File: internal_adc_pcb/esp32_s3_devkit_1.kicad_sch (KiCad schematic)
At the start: 2 parts, among them J1 Conn_01x22, J2 Conn_01x22

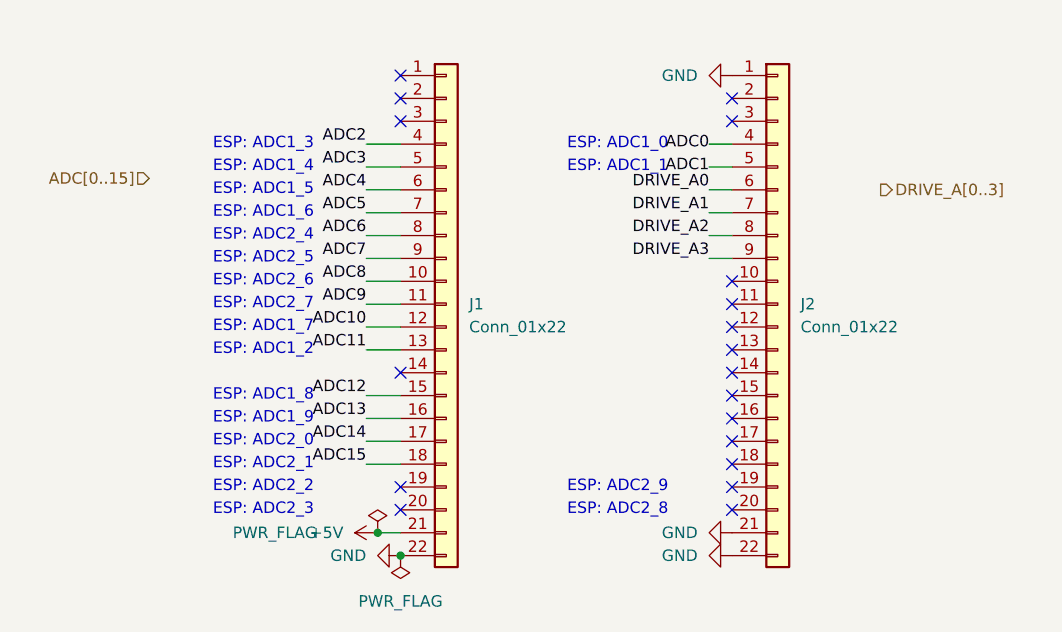
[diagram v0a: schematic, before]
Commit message: done all 4 TIA opamps for internal adc version
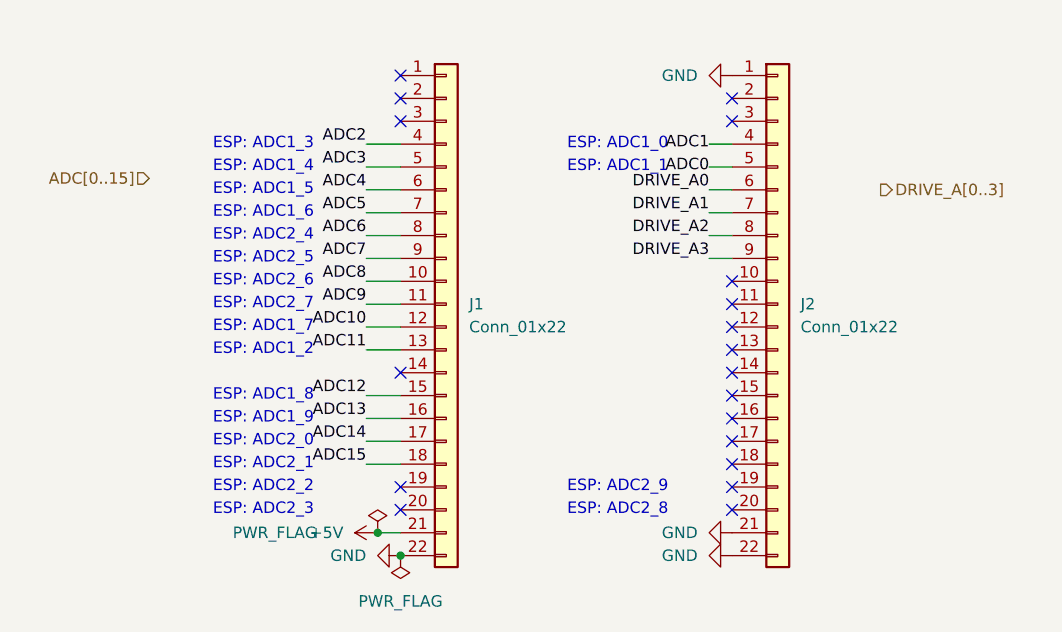
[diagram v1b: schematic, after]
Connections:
- net ADC0: now also J2.5 (Pin_5); no longer J2.4 (Pin_4)
- net ADC1: now also J2.4 (Pin_4); no longer J2.5 (Pin_5)
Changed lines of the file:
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@@
 		)
 	)
-	(label "ADC0"
+	(label "ADC1"
 		(at 92.71 64.77 180)
 		(effects
@@
 		)
 	)
-	(label "ADC1"
+	(label "ADC0"
 		(at 92.71 67.31 180)
 		(effects

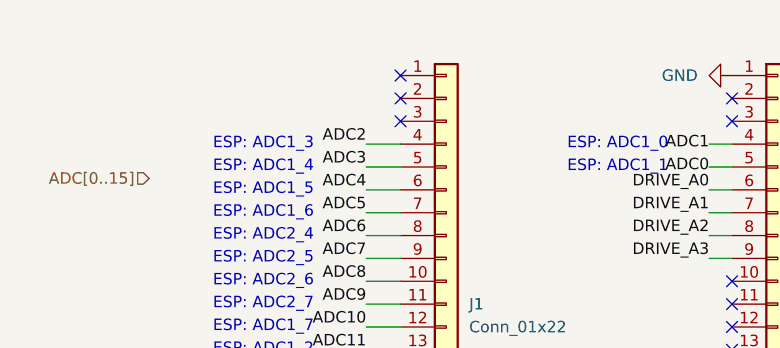
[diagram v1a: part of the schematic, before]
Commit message: fixing all ERC errors for internal ADC ver, fixing warnings now
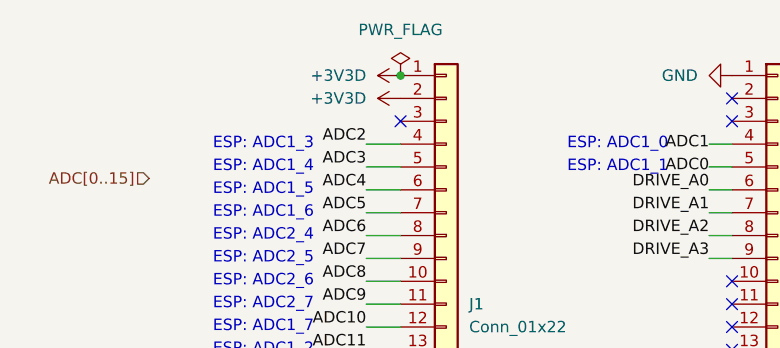
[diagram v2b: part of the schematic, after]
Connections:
- net +3V3D: now reaches J1.1 (Pin_1)
- net +3V3D: now also J1.2 (Pin_2)
- no-connect marks 19 -> 17
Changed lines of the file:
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@@
+	)
+	(junction
+		(at 58.42 57.15)
+		(diameter 0)
+		(color 0 0 0 0)
 	)
 	(junction
@@
 	(no_connect
 		(at 95.25 62.23)
-	)
-	(no_connect
-		(at 58.42 59.69)
-	)
-	(no_connect
-		(at 58.42 57.15)
 	)
 	(no_connect
@@
 	(symbol
 		(lib_id "power:PWR_FLAG")
+		(at 58.42 57.15 0)
+		(unit 1)
+		(body_style 1)
+		(exclude_from_sim no)
+		(in_bom yes)
+		(on_board yes)
+		(in_pos_files yes)
+		(dnp no)
+		(fields_autoplaced yes)
+		(property "Reference" "#FLG03"
+			(at 58.42 55.245 0)
+			(hide yes)
+			(show_name no)
+			(do_not_autoplace no)
+			(effects
+				(font
+					(size 1.27 1.27)
+				)
+			)
+		)
+		(property "Value" "PWR_FLAG"
+			(at 58.42 52.07 0)
+			(show_name no)
+			(do_not_autoplace no)
+			(effects
+				(font
+					(size 1.27 1.27)
+				)
+			)
+		)
+		(property "Footprint" ""
+			(at 58.42 57.15 0)
+			(hide yes)
+			(show_name no)
+			(do_not_autoplace no)
+			(effects
+				(font
+					(size 1.27 1.27)
+				)
+			)
+		)
+		(property "Datasheet" ""
+			(at 58.42 57.15 0)
+			(hide yes)
+			(show_name no)
+			(do_not_autoplace no)
+			(effects
+				(font
+					(size 1.27 1.27)
+				)
+			)
+		)
+		(property "Description" "Special symbol for telling ERC where power comes from"
+			(at 58.42 57.15 0)
+			(hide yes)
+			(show_name no)
+			(do_not_autoplace no)
+			(effects
+				(font
+					(size 1.27 1.27)
+				)
+			)
+		)
+		(pin "1"
+		)
+		(instances
+			(project "fsr_matrix_readout_internal_adc"
+				(path "/a2a8c34e-3adf-4a95-8857-b713f7048029/7b6125c2-c140-4f69-b2ce-c341fad458d4"
+					(reference "#FLG03")
+					(unit 1)
+				)
+			)
+		)
+	)
+	(symbol
+		(lib_id "power:PWR_FLAG")
 		(at 55.88 107.95 0)
 		(unit 1)
@@
 					(unit 1)
 				)
+			)
+		)
+	)
+	(symbol
+		(lib_id "power:+3V3")
+		(at 58.42 57.15 90)
+		(unit 1)
+		(body_style 1)
+		(exclude_from_sim no)
+		(in_bom yes)
+		(on_board yes)
+		(in_pos_files yes)
+		(dnp no)
+		(fields_autoplaced yes)
+		(property "Reference" "#PWR088"
+			(at 62.23 57.15 0)
+			(hide yes)
+			(show_name no)
+			(do_not_autoplace no)
+			(effects
+				(font
+					(size 1.27 1.27)
+				)
+			)
+		)
+		(property "Value" "+3V3D"
+			(at 54.61 57.1499 90)
+			(show_name no)
+			(do_not_autoplace no)
+			(effects
+				(font
+					(size 1.27 1.27)
+				)
+				(justify left)
+			)
+		)
+		(property "Footprint" ""
+			(at 58.42 57.15 0)
+			(hide yes)
+			(show_name no)
+			(do_not_autoplace no)
+			(effects
+				(font
+					(size 1.27 1.27)
+				)
+			)
+		)
+		(property "Datasheet" ""
+			(at 58.42 57.15 0)
+			(hide yes)
+			(show_name no)
+			(do_not_autoplace no)
+			(effects
+				(font
+					(size 1.27 1.27)
+				)
+			)
+		)
+		(property "Description" "Power symbol creates a global label with name \"+3V3\""
+			(at 58.42 57.15 0)
+			(hide yes)
+			(show_name no)
+			(do_not_autoplace no)
+			(effects
+				(font
+					(size 1.27 1.27)
+				)
+			)
+		)
+		(pin "1"
+		)
+		(instances
+			(project "fsr_matrix_readout_internal_adc"
+				(path "/a2a8c34e-3adf-4a95-8857-b713f7048029/7b6125c2-c140-4f69-b2ce-c341fad458d4"
+					(reference "#PWR088")
+					(unit 1)
+				)
+			)
+		)
+	)
+	(symbol
+		(lib_id "power:+3V3")
+		(at 58.42 59.69 90)
+		(unit 1)
+		(body_style 1)
+		(exclude_from_sim no)
+		(in_bom yes)
+		(on_board yes)
+		(in_pos_files yes)
+		(dnp no)
+		(fields_autoplaced yes)
+		(property "Reference" "#PWR089"
+			(at 62.23 59.69 0)
+			(hide yes)
+			(show_name no)
+			(do_not_autoplace no)
+			(effects
+				(font
+					(size 1.27 1.27)
+				)
+			)
+		)
+		(property "Value" "+3V3D"
+			(at 54.61 59.6899 90)
+			(show_name no)
+			(do_not_autoplace no)
+			(effects
+				(font
+					(size 1.27 1.27)
+				)
+				(justify left)
+			)
+		)
+		(property "Footprint" ""
+			(at 58.42 59.69 0)
+			(hide yes)
+			(show_name no)
+			(do_not_autoplace no)
+			(effects
+				(font
+					(size 1.27 1.27)
+				)
+			)
+		)
+		(property "Datasheet" ""
+			(at 58.42 59.69 0)
+			(hide yes)
+			(show_name no)
+			(do_not_autoplace no)
+			(effects
+				(font
+					(size 1.27 1.27)
+				)
+			)
+		)
+		(property "Description" "Power symbol creates a global label with name \"+3V3\""
+			(at 58.42 59.69 0)
+			(hide yes)
+			(show_name no)
+			(do_not_autoplace no)
+			(effects
+				(font
+					(size 1.27 1.27)
+				)
+			)
+		)
+		(pin "1"
+		)
+		(instances
+			(project "fsr_matrix_readout_internal_adc"
+				(path "/a2a8c34e-3adf-4a95-8857-b713f7048029/7b6125c2-c140-4f69-b2ce-c341fad458d4"
+					(reference "#PWR089")
+					(unit 1)
+				)

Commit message: change ESP connector from pin to socket
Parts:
- J1, J2: footprint Connector_PinHeader_2.54mm:PinHeader_1x22_P2.54mm_Vertical -> Connector_PinSocket_2.54mm:PinSocket_1x22_P2.54mm_Vertical
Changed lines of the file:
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@@
 			)
 		)
-		(property "Footprint" "Connector_PinHeader_2.54mm:PinHeader_1x22_P2.54mm_Vertical"
+		(property "Footprint" "Connector_PinSocket_2.54mm:PinSocket_1x22_P2.54mm_Vertical"
 			(at 100.33 82.55 0)
 			(hide yes)
@@
 			)
 		)
-		(property "Footprint" "Connector_PinHeader_2.54mm:PinHeader_1x22_P2.54mm_Vertical"
+		(property "Footprint" "Connector_PinSocket_2.54mm:PinSocket_1x22_P2.54mm_Vertical"
 			(at 63.5 82.55 0)
 			(hide yes)
